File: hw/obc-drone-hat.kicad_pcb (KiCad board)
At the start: 2 copper layers, 65 x 56.5 mm, 66 parts, among them SW1 SW_DIP_x04

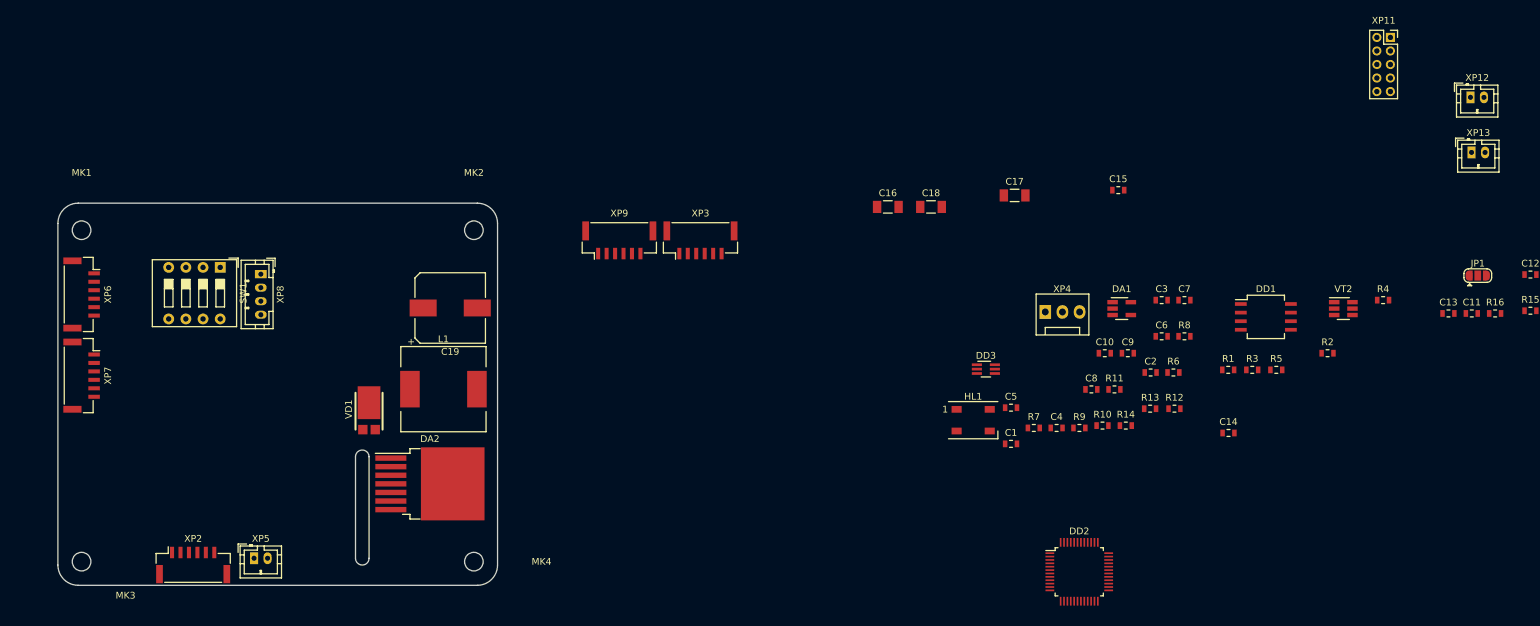
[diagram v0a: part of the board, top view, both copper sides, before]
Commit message: hw: add servo conn
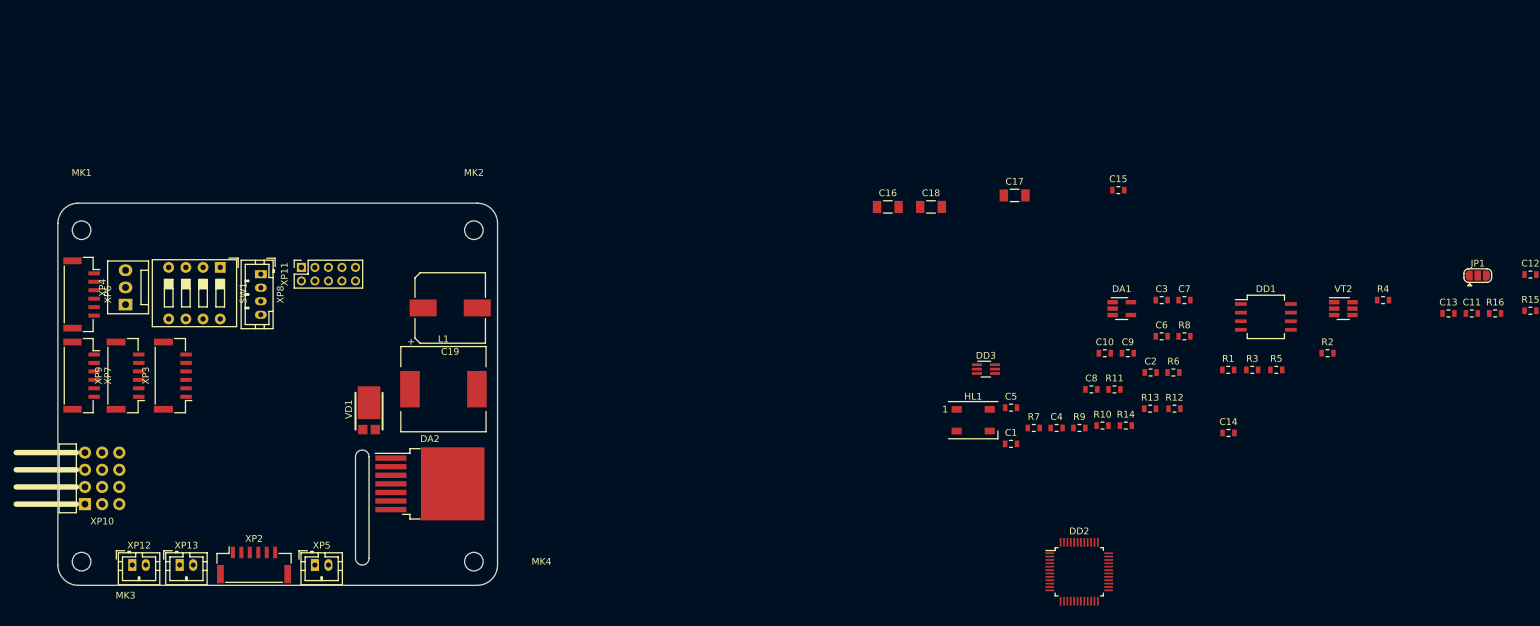
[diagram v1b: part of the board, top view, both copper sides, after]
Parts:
- added XP10: SERVO, hat:SERVO4, F.Cu at (134.0, 128.0)
- moved XP12 209.6 mm to (141.0, 137.0)
- moved XP13 200.5 mm to (148.0, 137.0)
- moved XP11 164.6 mm to (166.0, 93.0), turned to 90 degrees
- moved XP4 136.0 mm to (140.0, 98.5), turned to 90 degrees
- moved XP3 80.5 mm to (147.0, 109.0), turned to 90 degrees
- moved XP9 75.7 mm to (140.0, 109.0), turned to 90 degrees
- moved XP5 9.06 mm to (168.0, 137.0)
- moved XP2 9.00 mm to (159.0, 137.0)
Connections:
- DD2 pad 27: (no net) -> SERVO2
- DD2 pad 28: (no net) -> SERVO1
- DD2 pad 29: (no net) -> SERVO0
- DD2 pad 32: (no net) -> SERVO3

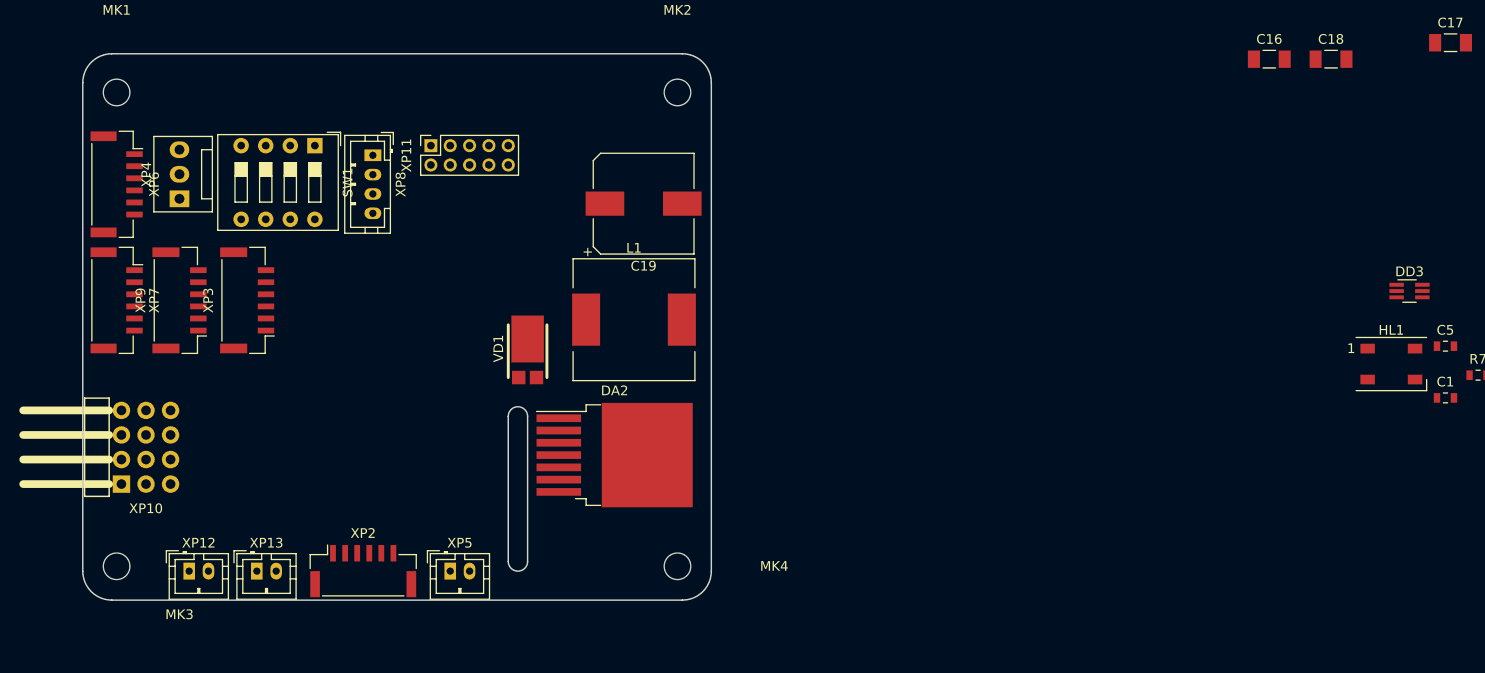
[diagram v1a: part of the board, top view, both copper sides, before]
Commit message: hw: add battery input connector
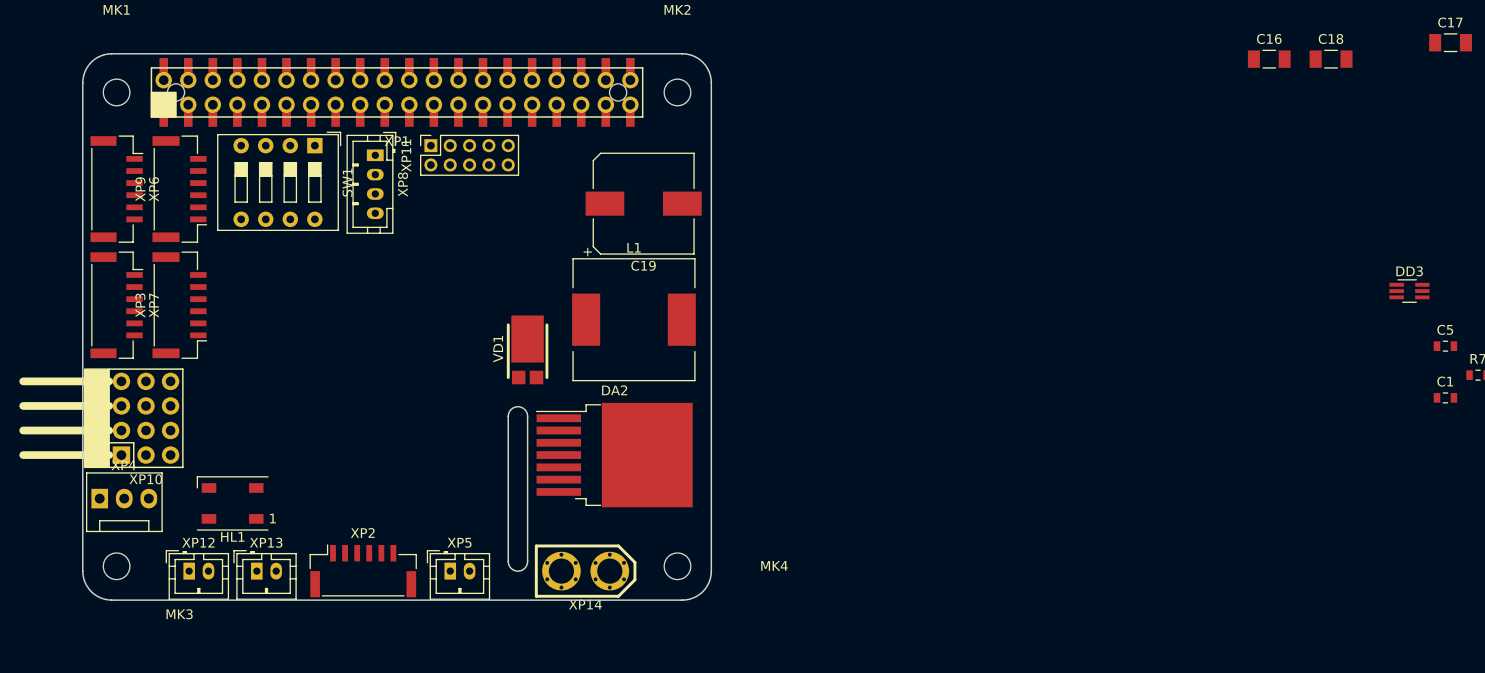
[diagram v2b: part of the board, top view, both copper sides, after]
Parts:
- added XP1: Rpi_40PIN, hat:RaspberryPi-40Pin_P2.54mm, F.Cu at (162.5, 87.5)
- added XP14: BATT, hat:XT30, F.Cu at (182.0, 137.0)
- moved HL1 120.7 mm to (145.5, 130.0), turned to 180 degrees
- moved XP4 32.1 mm to (131.8, 129.5), turned to 0 degrees
- moved XP9 11.5 mm to (140.0, 97.5)
- moved XP3 7.02 mm to (140.0, 109.5)
- moved XP10 3.00 mm to (134.0, 125.0)
- moved XP6 0.50 mm to (133.5, 97.5)
- moved XP7 0.50 mm to (133.5, 109.5)
- moved XP8 0.25 mm to (160.2, 94.0)
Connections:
- net ADC_Vbat renamed Vbat
- net Net-(C15-Pad2) renamed /DC-DC/CB
- C19 pad 1: ADC_V5hat -> +5Vhat
- C8 pad 1: ADC_V5hat -> +5Vhat
- DA2 pad 6: ADC_V5hat -> +5Vhat
- DD2 pad 14: (no net) -> ~RPI_SPI0_CE1
- DD2 pad 18: (no net) -> ~STM_INT
- DD2 pad 7: (no net) -> ~STM_RESET
- DD4 pad 5: (no net) -> ~RPI_SPI0_CE0
- HL1 pad 1: ADC_V5hat -> +5Vhat
- L1 pad 2: ADC_V5hat -> +5Vhat
- R13 pad 1: ADC_V5hat -> +5Vhat
- R9 pad 1: ADC_V5hat -> +5Vhat
- VT1 pad 3: ADC_V5hat -> +5Vhat
- VT2 pad 6: ADC_V5hat -> +5Vhat
- VT3 pad 2: ADC_V5hat -> +5Vhat
- XP10 pad 11: ADC_V5hat -> +5Vhat
- XP10 pad 2: ADC_V5hat -> +5Vhat
- XP10 pad 5: ADC_V5hat -> +5Vhat
- XP10 pad 8: ADC_V5hat -> +5Vhat
- XP11 pad 1: (no net) -> BCM5
- XP11 pad 2: (no net) -> BCM12
- XP11 pad 3: (no net) -> BCM6
- XP11 pad 4: (no net) -> ~RPI_SPI1_CE2
- XP11 pad 5: (no net) -> BCM13
- XP11 pad 6: (no net) -> BCM20_SPI1_MOSI
- XP11 pad 7: (no net) -> BCM19_SPI1_MISO
- XP11 pad 8: (no net) -> BCM21_SPI1_SCLK
- XP11 pad 9: (no net) -> BCM26
- XP12 pad 2: ADC_V5hat -> +5Vhat
- XP13 pad 2: ADC_V5hat -> +5Vhat
- XP6 pad 1: ADC_V5hat -> +5Vhat
- XP7 pad 1: ADC_V5hat -> +5Vhat
- XP9 pad 1: ADC_V5hat -> +5VP
- XP9 pad 2: (no net) -> RPI_TX
- XP9 pad 3: (no net) -> RPI_RX

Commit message: hw: placement of bigger components
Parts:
- moved DD4 168.2 mm to (196.9, 61.2)
- moved DD5 168.2 mm to (210.1, 63.7)
- moved ZQ1 168.2 mm to (183.4, 60.3)
- moved C1 147.4 mm to (139.9, 51.6)
- moved C4 147.4 mm to (146.7, 49.2)
- moved C5 147.4 mm to (139.9, 46.2)
- moved R10 147.4 mm to (153.4, 48.9)
- moved R16 147.4 mm to (211.5, 32.3)
- moved R7 147.4 mm to (143.3, 49.2)
- moved VT1 147.4 mm to (237.5, 49.0)
- moved VT3 147.4 mm to (237.5, 59.1)
- moved C10 147.4 mm to (153.8, 38.2)
- moved C12 147.4 mm to (216.7, 26.6)
- moved C13 147.4 mm to (204.6, 32.3)
- moved C14 147.4 mm to (172.1, 50.0)
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
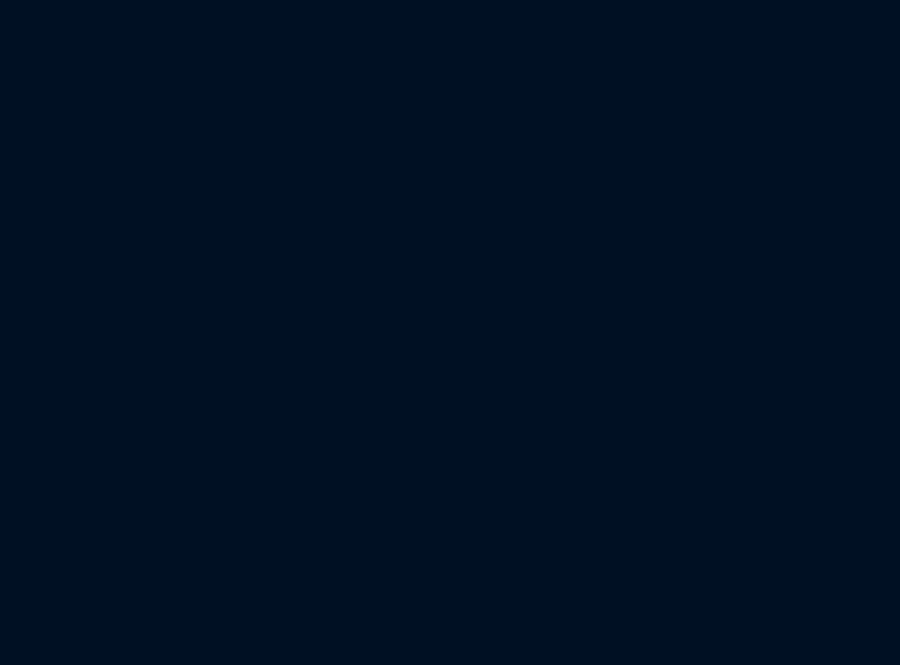
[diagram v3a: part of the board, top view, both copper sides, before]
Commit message: hw: connect GH mount points with GND, add 3V battery
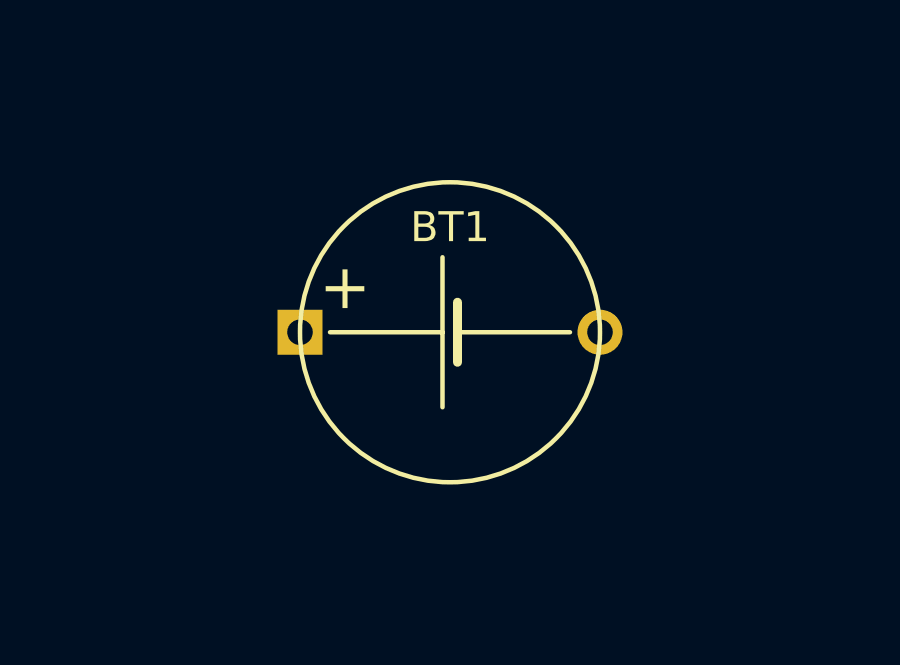
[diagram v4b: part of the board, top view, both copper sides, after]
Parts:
- added BT1: CR1225-VBY2, hat:CR1225-VBY2, F.Cu at (212.8, 82.5)
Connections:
- DD5 pad 14: (no net) -> Net-(BT1-Pad1)
- XP2 pad MP: (no net) -> GND
- XP3 pad MP: (no net) -> GND
- XP6 pad MP: (no net) -> GND
- XP7 pad MP: (no net) -> GND
- XP9 pad MP: (no net) -> GND

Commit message: hw: move passives
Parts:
- moved VT3 136.2 mm to (122.5, 132.0)
- moved R15 120.1 mm to (123.0, 107.0)
- moved C12 118.6 mm to (126.5, 103.5)
- moved C3 115.5 mm to (159.7, 145.8)
- moved C7 115.5 mm to (163.1, 145.8)
- moved R16 113.5 mm to (123.1, 103.5)
- moved VT1 112.7 mm to (128.0, 75.5)
- moved C6 110.5 mm to (156.0, 146.0)
- moved C13 108.1 mm to (126.5, 107.0)
- moved R12 105.0 mm to (144.5, 149.5)
- moved C5 103.5 mm to (167.5, 146.0)
- moved R14 102.2 mm to (175.0, 149.5)
- moved DA1 99.5 mm to (152.0, 131.0), turned to 270 degrees
- moved C8 99.0 mm to (200.0, 130.0)
- moved DD3 97.0 mm to (170.0, 131.5)
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
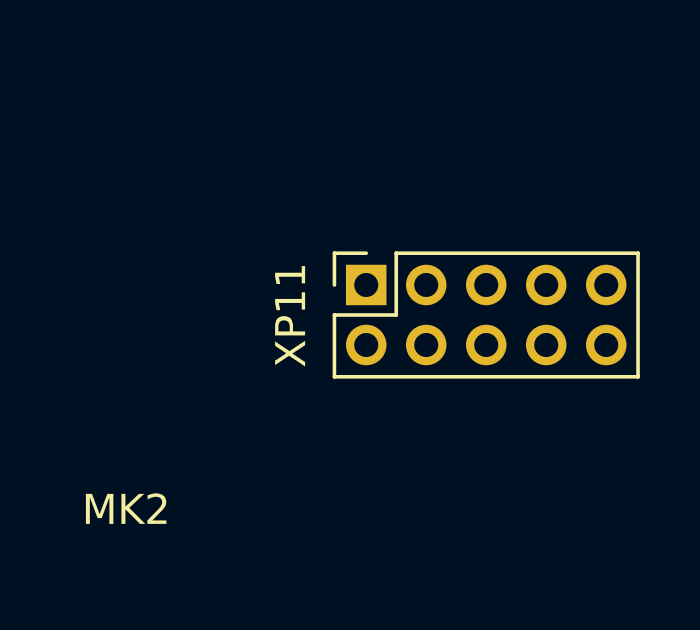
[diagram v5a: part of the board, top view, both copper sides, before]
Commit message: hw: remove header with unused rpi gpio's, more net labels
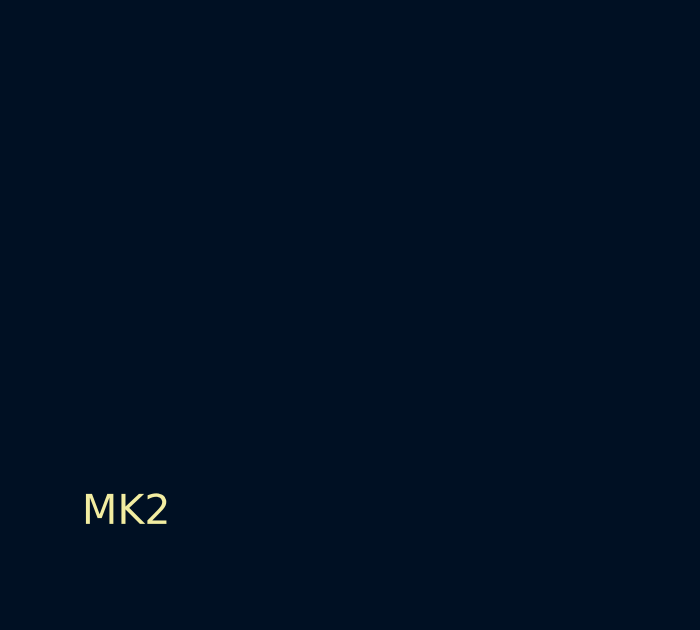
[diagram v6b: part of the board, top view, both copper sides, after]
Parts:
- removed XP11: UNUSED PINS, Connector_PinSocket_2.00mm:PinSocket_2x05_P2.00mm_Vertical
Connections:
- net Net-(BT1-Pad1) renamed /RTC/+3Vbat
- net Net-(C13-Pad1) renamed /UART/U_V18
- XP1 pad 29: BCM5 -> Net-(XP1-Pad29)
- XP1 pad 31: BCM6 -> Net-(XP1-Pad31)
- XP1 pad 32: BCM12 -> Net-(XP1-Pad32)
- XP1 pad 33: BCM13 -> Net-(XP1-Pad33)
- XP1 pad 35: BCM19_SPI1_MISO -> Net-(XP1-Pad35)
- XP1 pad 36: ~RPI_SPI1_CE2 -> Net-(XP1-Pad36)
- XP1 pad 37: BCM26 -> Net-(XP1-Pad37)
- XP1 pad 38: BCM20_SPI1_MOSI -> Net-(XP1-Pad38)
- XP1 pad 40: BCM21_SPI1_SCLK -> Net-(XP1-Pad40)
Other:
- copper layers 2 -> 4

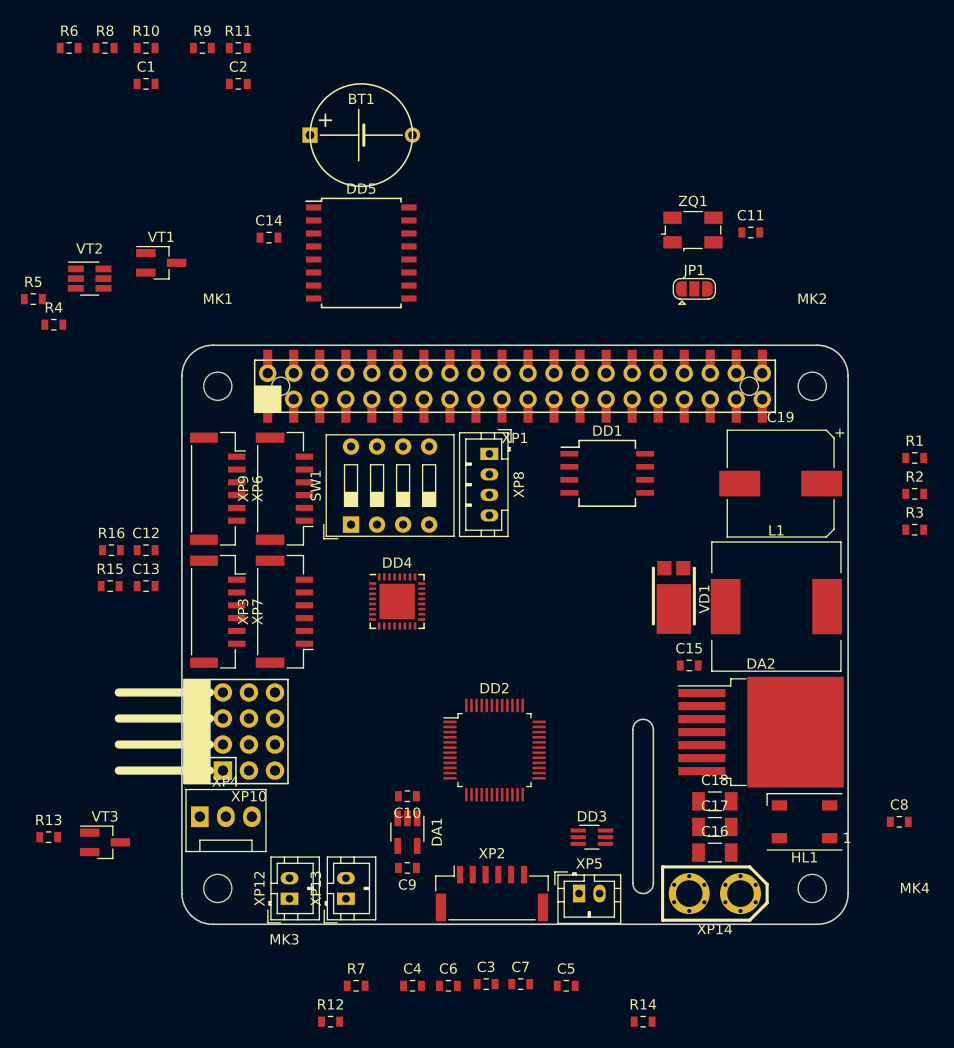
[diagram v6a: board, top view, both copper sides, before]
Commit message: hw: place all components. remove C7 0.1 coupling as not needed.
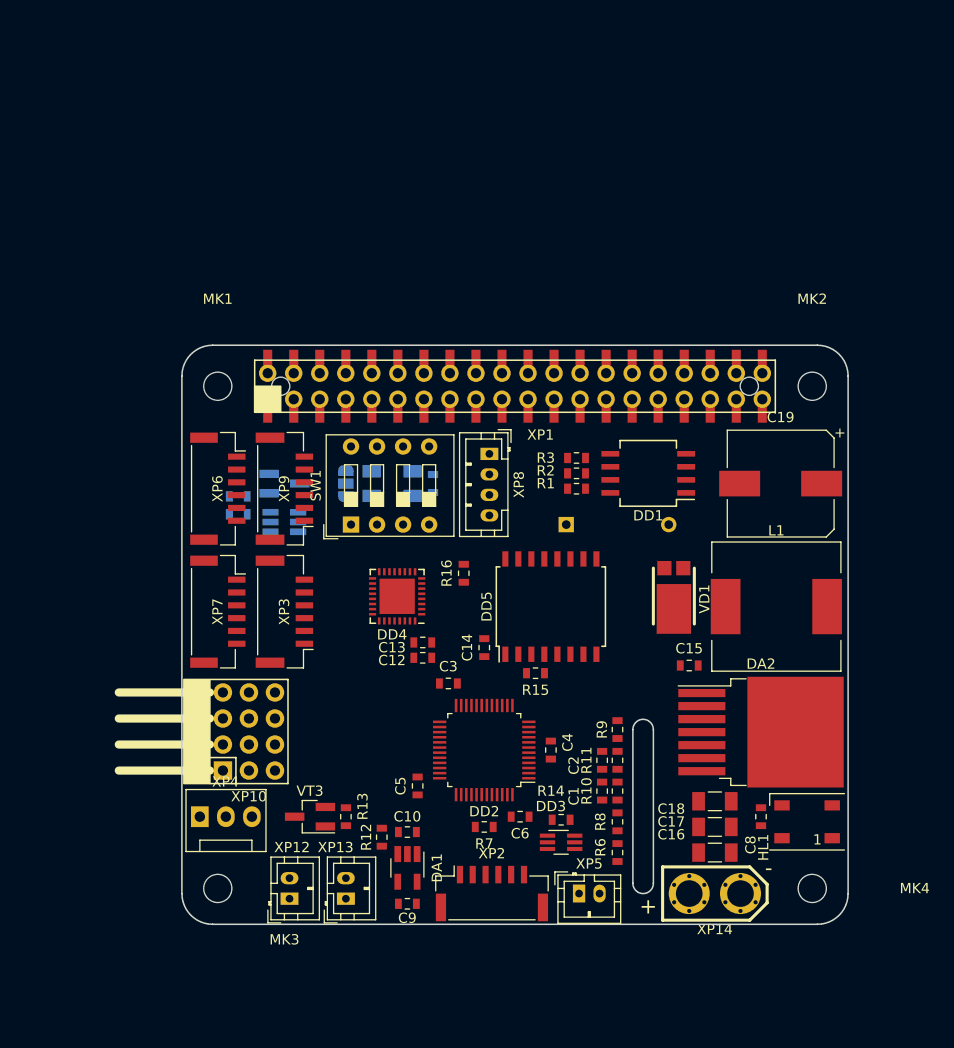
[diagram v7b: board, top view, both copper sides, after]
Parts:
- removed C7: 0.1, Capacitor_SMD:C_0603_1608Metric
- BT1, C11, JP1, R4, R5, VT1, VT2, ZQ1: moved to B.Cu
- moved R6 95.0 mm to (172.5, 133.0), turned to 90 degrees
- moved R8 90.6 mm to (172.5, 130.0), turned to 90 degrees
- moved R10 85.9 mm to (172.5, 127.0), turned to 90 degrees
- moved C1 82.1 mm to (171.0, 127.0), turned to 90 degrees
- moved R11 78.7 mm to (172.5, 124.0), turned to 270 degrees
- moved R9 77.9 mm to (172.5, 121.0), turned to 270 degrees
- moved C2 74.9 mm to (171.0, 124.0), turned to 270 degrees
- moved BT1 45.5 mm to (172.5, 101.0)
- moved C14 45.2 mm to (159.5, 113.0), turned to 90 degrees
- moved R15 42.4 mm to (164.5, 115.5), turned to 180 degrees
- moved C11 39.5 mm to (154.5, 97.0), turned to 270 degrees
- moved DD5 39.1 mm to (166.0, 109.0), turned to 90 degrees
- moved JP1 38.9 mm to (146.0, 97.0), turned to 270 degrees
- moved ZQ1 38.4 mm to (150.5, 97.0), turned to 180 degrees
- moved R16 34.4 mm to (157.5, 105.8), turned to 90 degrees
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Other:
- board text added: "+"
- board text added: "-"
